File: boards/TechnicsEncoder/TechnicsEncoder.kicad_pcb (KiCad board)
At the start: 2 copper layers, 110 x 53 mm, 33 parts, among them J1 ISP, J2 Bender, J3 Technics, J4 SelectRX, J5 MIDI In, J6 MIDI Out, J7 BoardCon, J8 PistonEncoder, U1 ATmega48-20P, U2 6N137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

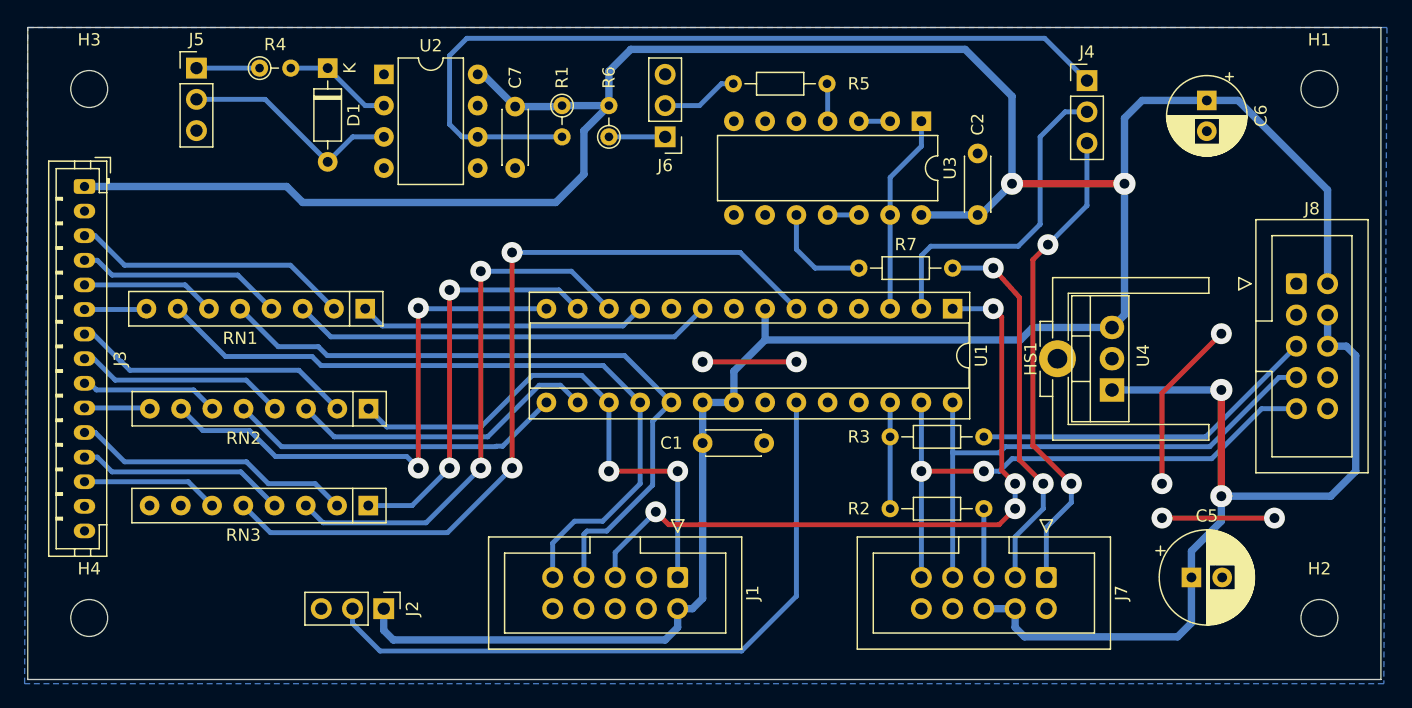
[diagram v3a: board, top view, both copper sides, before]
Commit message: Fixed interrupt line to use open collector, added pullups to I2C lines
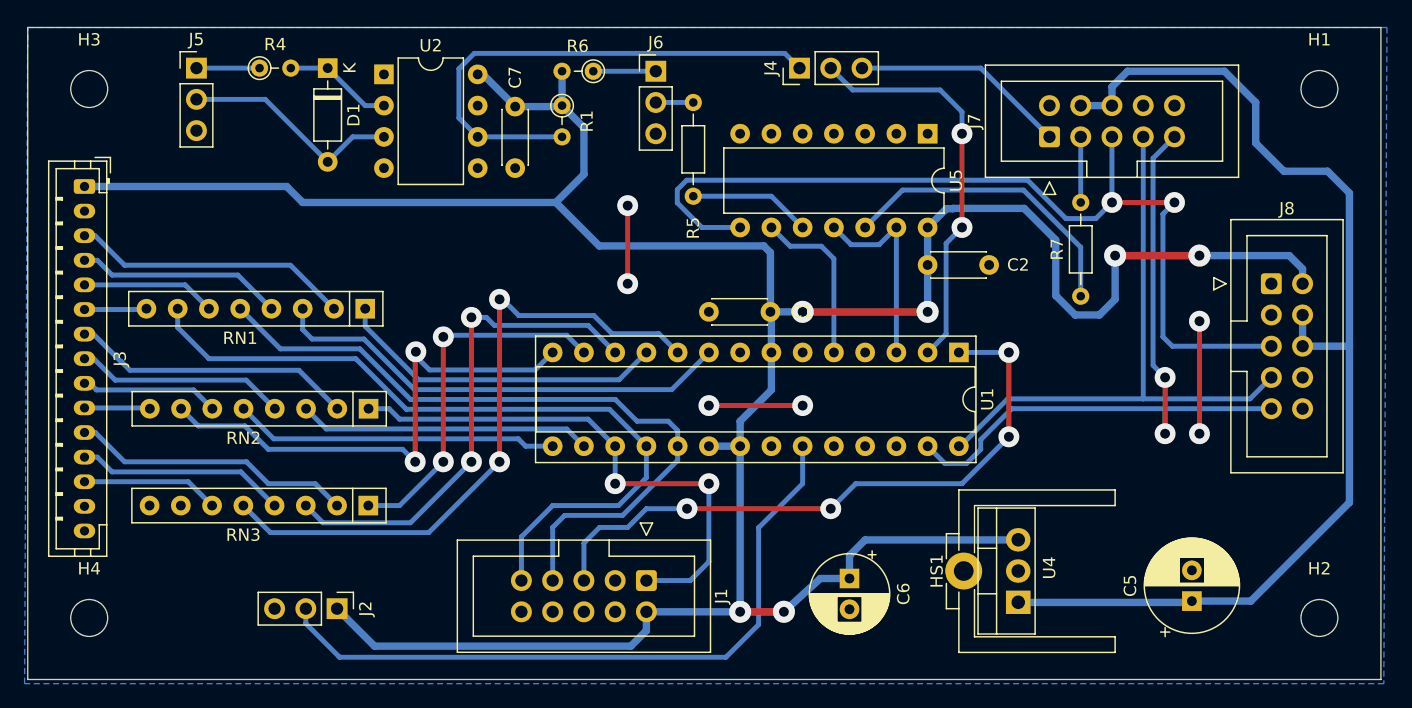
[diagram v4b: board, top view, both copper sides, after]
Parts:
- removed R2, R3: 220, Resistor_THT:R_Axial_DIN0204_L3.6mm_D1.6mm_P7.62mm_Horizontal
- removed U3: 74LS14, Package_DIP:DIP-14_W7.62mm
- added U5: 74LS07, Package_DIP:DIP-14_W7.62mm, F.Cu at (149.1, 73.7)
- moved C6 48.5 mm to (142.7, 109.8)
- moved J7 35.8 mm to (159.0, 73.9), turned to 90 degrees
- moved J4 23.4 mm to (138.7, 68.3), turned to 90 degrees
- moved HS1 18.9 mm to (152.9, 109.2)
- moved U4 18.9 mm to (156.5, 111.7)
- moved R7 18.2 mm to (161.5, 86.9), turned to 90 degrees
- moved R5 14.2 mm to (130.0, 78.7), turned to 90 degrees
- moved C1 12.0 mm to (136.3, 88.1), turned to 180 degrees
- moved C2 5.75 mm to (149.1, 84.3), turned to 0 degrees
- moved R6 5.48 mm to (121.9, 68.6), turned to 180 degrees
- moved J6 5.39 mm to (127.0, 68.6), turned to 0 degrees
- moved J2 3.80 mm to (101.1, 112.3)
- moved U1 3.59 mm to (151.6, 91.4)
- moved J1 2.55 mm to (126.2, 110.0)
- moved J8 2.03 mm to (177.0, 85.9)
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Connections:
- J8 pad 5: Net-(J8-Pin_5) -> Net-(J7-Pin_5)
- U1 pad 10: unconnected-(U1-XTAL2/PB7-Pad10) -> Read
- U1 pad 26: Interrupt -> unconnected-(U1-PC3-Pad26)
- U1 pad 5: unconnected-(U1-PD3-Pad5) -> Interrupt
- U1 pad 6: Read -> unconnected-(U1-PD4-Pad6)
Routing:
- net Net-(J7-Pin_5): track 5.59 -> 75.4 mm, vias 0 -> 2
- net Net-(J8-Pin_5): track 28.5 -> 0.00 mm
- net MIDI Rx: track 69.0 -> 41.7 mm
- net TXD_OUT: track 31.1 -> 5.84 mm, vias 2 -> 0
- net Net-(J4-Pin_3): track 39.3 -> 17.6 mm, vias 2 -> 0
- net +5V: track 253.3 -> 234.9 mm, vias 2 -> 6
- net +12V: track 74.3 -> 92.0 mm, vias 2 -> 0
- net Net-(R7-Pad1): track 8.51 -> 24.7 mm
- net Read: track 67.5 -> 54.1 mm
- net SDA: track 46.8 -> 58.1 mm
- net GND: track 31.0 -> 23.1 mm
- net Net-(R5-Pad1): track 3.00 -> 9.94 mm
- net RXD: track 26.8 -> 32.9 mm, vias 0 -> 2
- net Interrupt: track 8.64 -> 13.8 mm
- net Reset: track 57.2 -> 52.1 mm
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
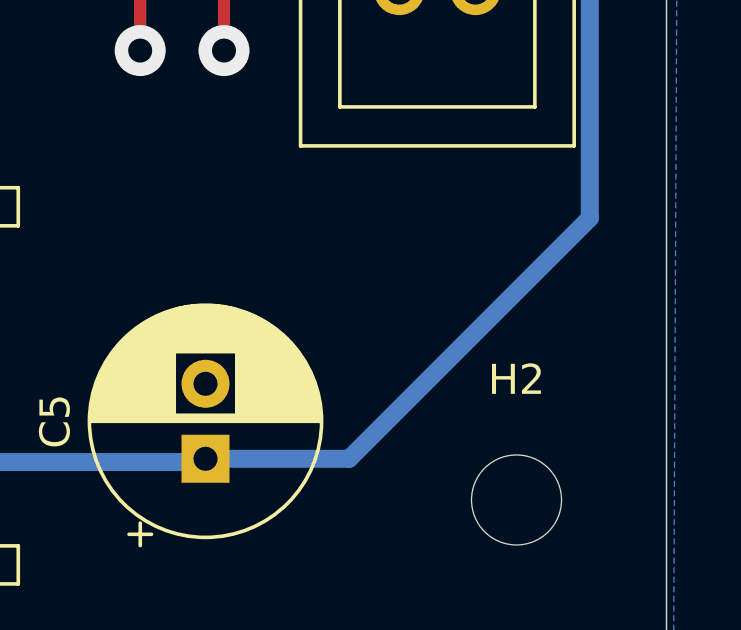
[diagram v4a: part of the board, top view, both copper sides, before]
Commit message: Added bypass caps to power supplies, use cheaper MAX232 IC.
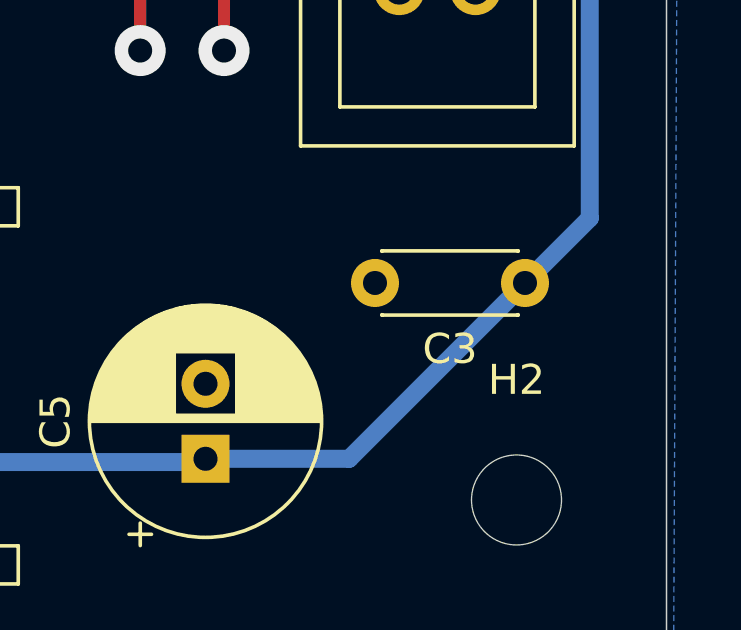
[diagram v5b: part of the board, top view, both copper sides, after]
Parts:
- added C3: 330nF, Capacitor_THT:C_Disc_D4.3mm_W1.9mm_P5.00mm, F.Cu at (181.2, 105.8)
- RN1, RN2, RN3: value R_Pack04 -> 220

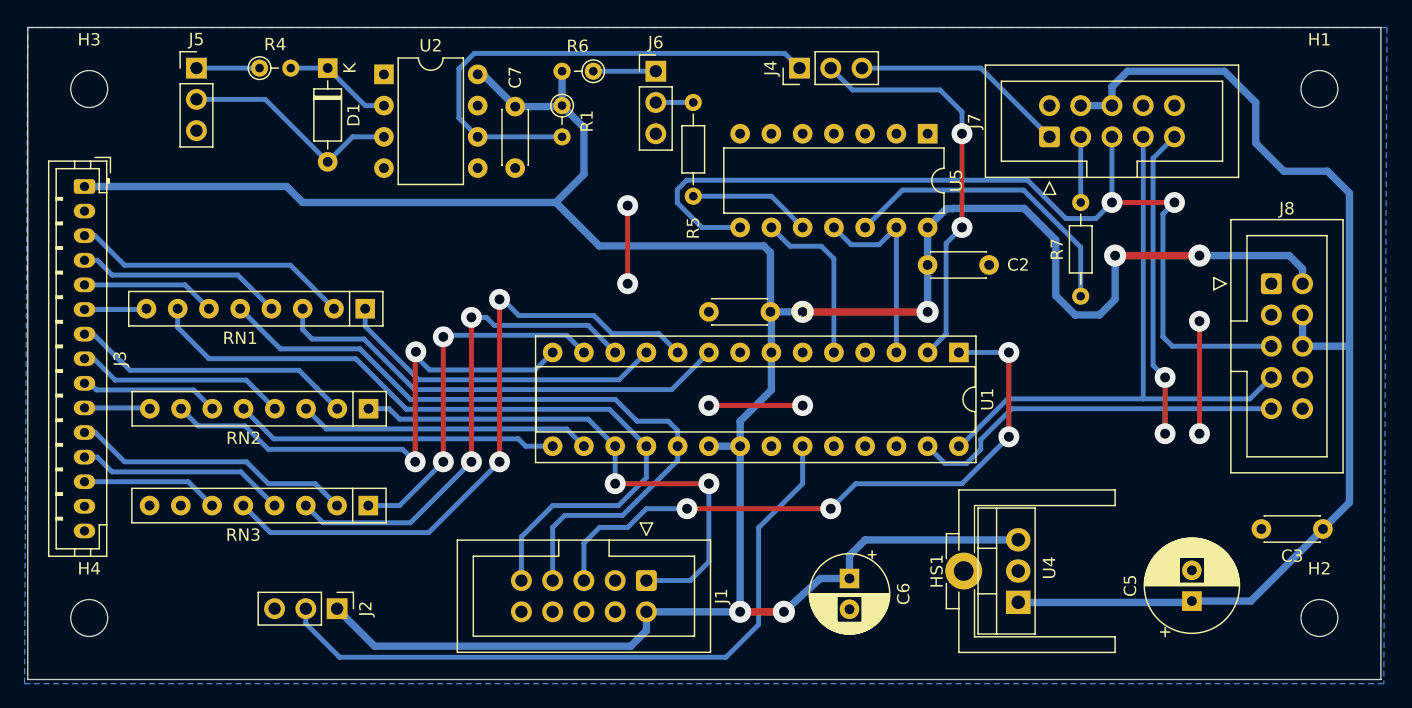
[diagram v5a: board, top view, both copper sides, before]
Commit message: Updated design rules to 0.32mm template and exported Gerber files
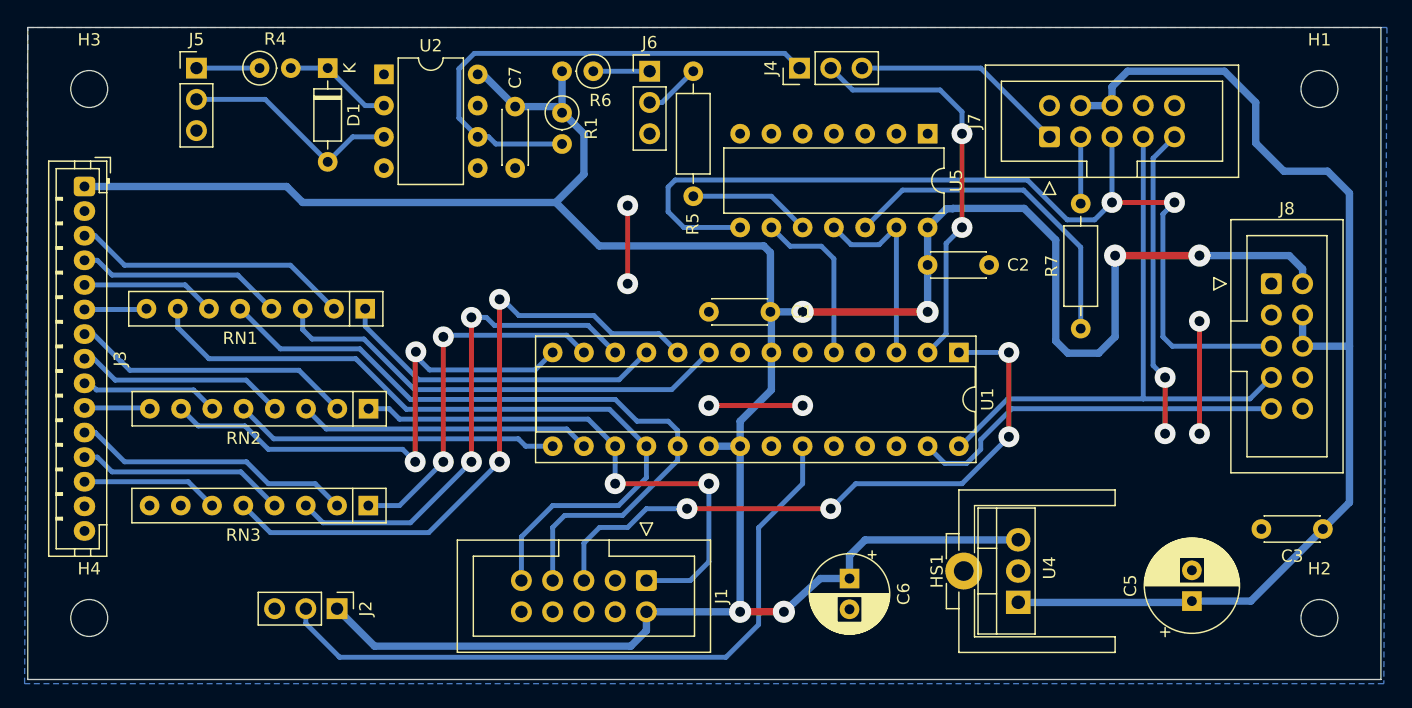
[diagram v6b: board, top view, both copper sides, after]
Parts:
- R1, R4, R6: footprint Resistor_THT:R_Axial_DIN0204_L3.6mm_D1.6mm_P2.54mm_Vertical -> Resistor_THT:R_Axial_DIN0207_L6.3mm_D2.5mm_P2.54mm_Vertical
- R5, R7: footprint Resistor_THT:R_Axial_DIN0204_L3.6mm_D1.6mm_P7.62mm_Horizontal -> Resistor_THT:R_Axial_DIN0207_L6.3mm_D2.5mm_P10.16mm_Horizontal
- moved R7 2.63 mm to (161.5, 89.5)
- moved R1 0.58 mm to (119.4, 72.0)
- moved J6 0.50 mm to (126.5, 68.6)
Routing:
- net +5V: track 234.9 -> 241.2 mm
- net Net-(R7-Pad1): track 24.7 -> 27.3 mm
- net Net-(J7-Pin_5): track 75.4 -> 77.5 mm
- net Net-(J6-Pin_2): track 3.05 -> 4.10 mm
